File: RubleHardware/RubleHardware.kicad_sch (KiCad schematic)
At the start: 46 parts, among them IC1 LTC3780EUH#PBF, J1_IN1 Conn_01x08_Male, J2_OUT1 Conn_01x08_Male

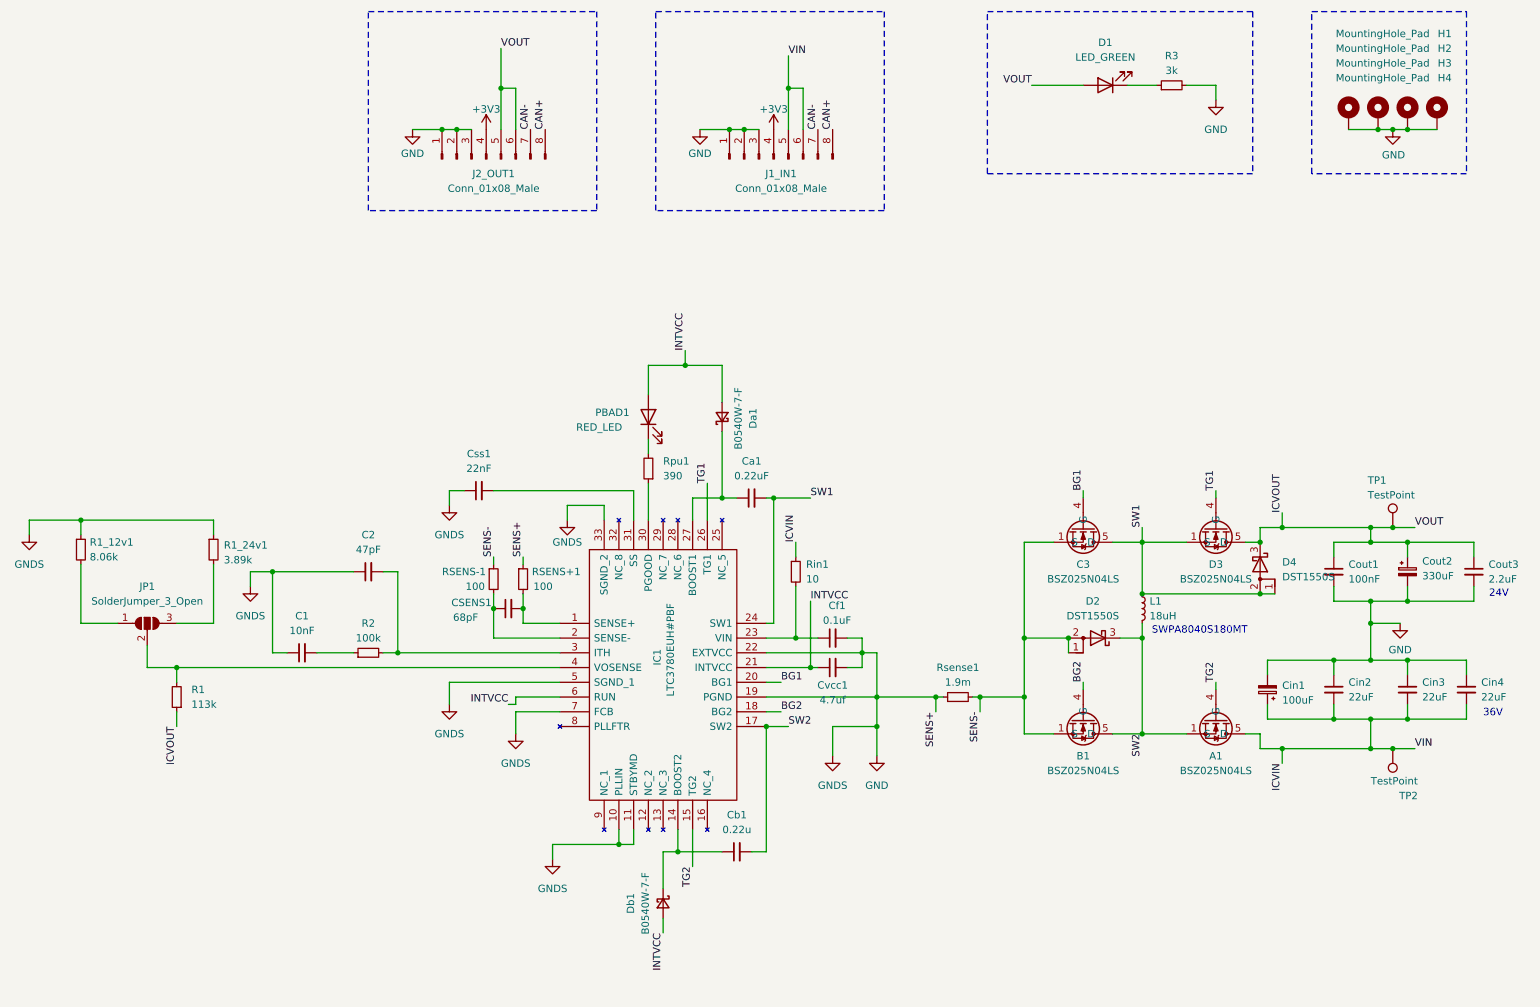
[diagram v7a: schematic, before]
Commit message: feat: V2.0 changes to schematic
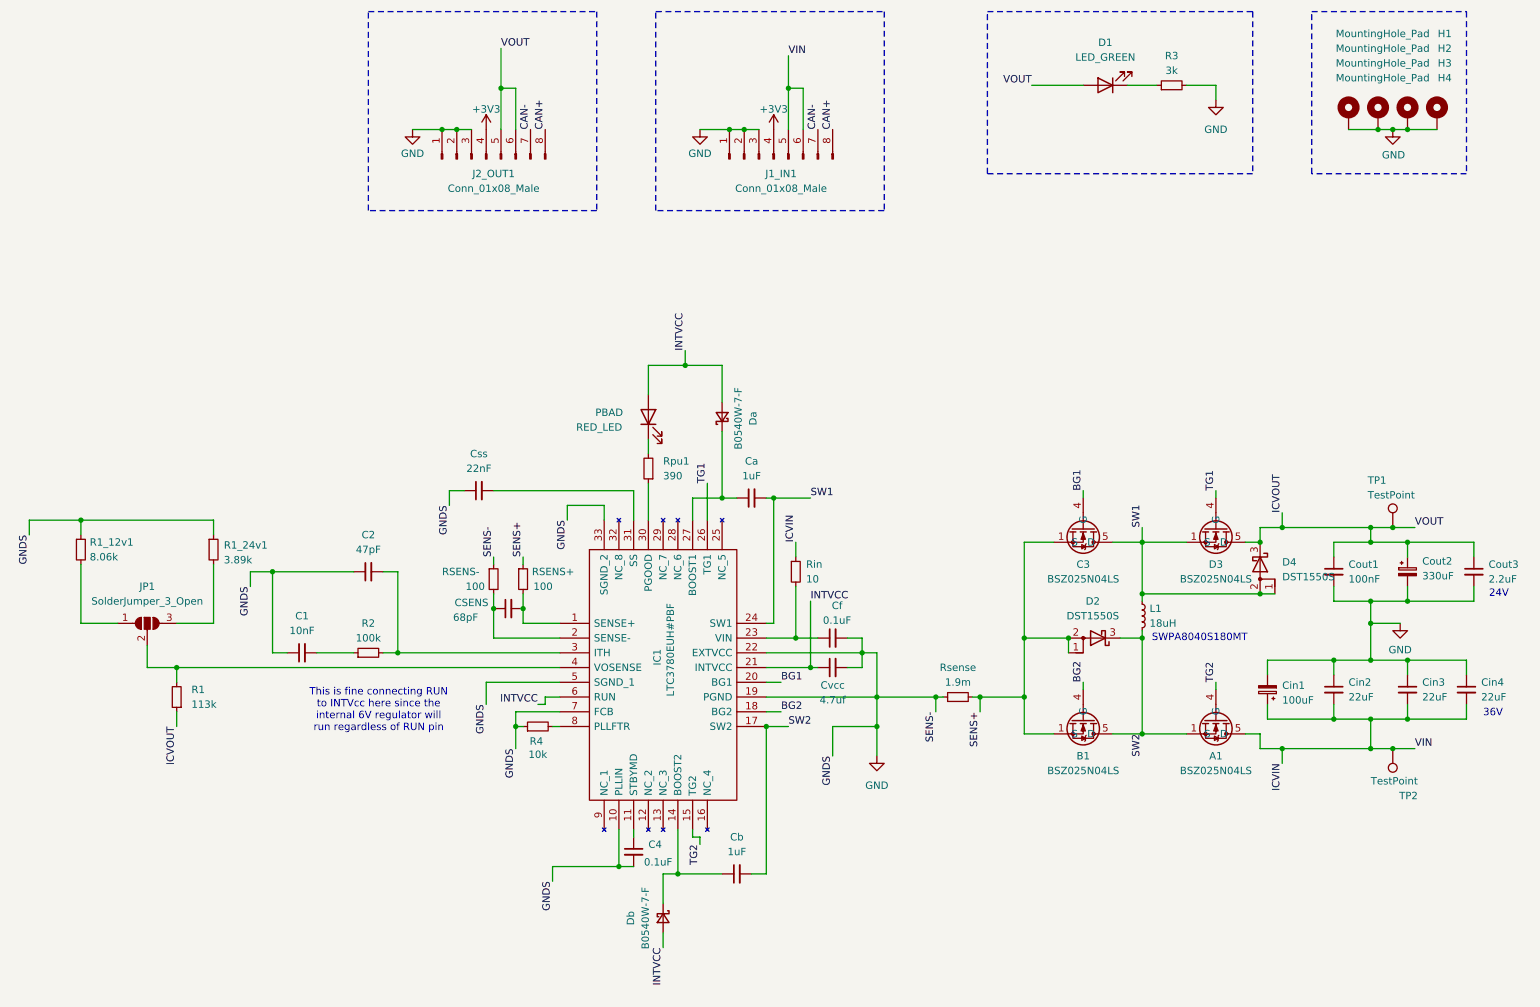
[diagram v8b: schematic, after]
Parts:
- added C4: 0.1uF, symbol Device:C_Small
- added R4: 10k, symbol Device:R_Small
- Ca: renamed from Ca1; value 0.22uF -> 1uF
- Cb: renamed from Cb1; value 0.22u -> 1uF
- renumbered CSENS1 to CSENS, Cf1 to Cf, Css1 to Css, Cvcc1 to Cvcc, Da1 to Da, Db1 to Db, PBAD1 to PBAD, RSENS+1 to RSENS+, RSENS-1 to RSENS-, Rin1 to Rin, Rsense1 to Rsense
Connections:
- net GND: now also RSENS-.1, C4.2, R4.1; no longer IC1.11 (STBYMD), RSENS+.1
- net at IC1.8 (PLLFTR): now also R4.2
- net SENS- renamed SENS+
- net SENS+: now also RSENS+.1; no longer RSENS-.1
- new net: C4.1, IC1.11 (STBYMD)
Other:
- note added: "This is fine connecting RUN to INTVcc here since the internal 6V regulator will run regardless of RUN pin"
- moved on the sheet: Cb, Db, L1
